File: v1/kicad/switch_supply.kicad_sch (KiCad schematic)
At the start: 12 parts, among them U11 ADG419BN, U12 ADG419BN, U7 ADG419BN

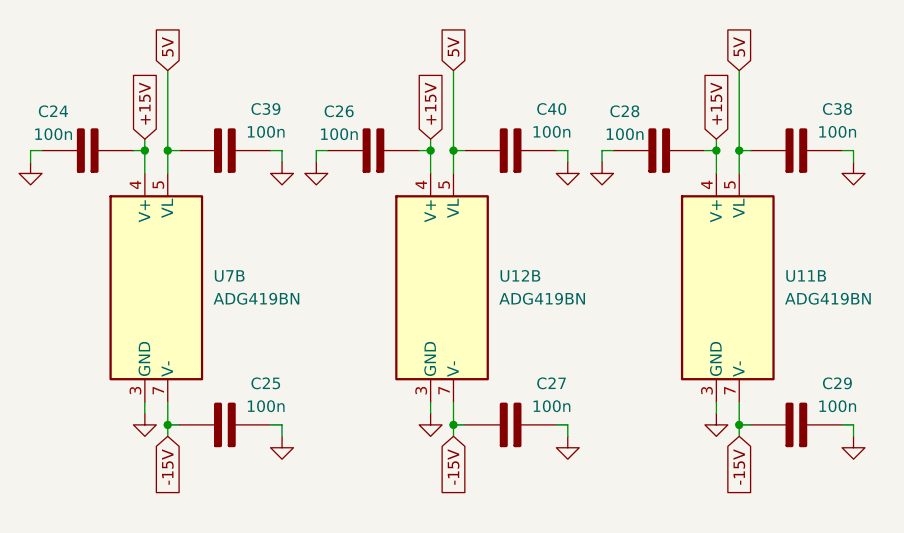
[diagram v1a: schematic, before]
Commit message: Adding KiKit multiboarding
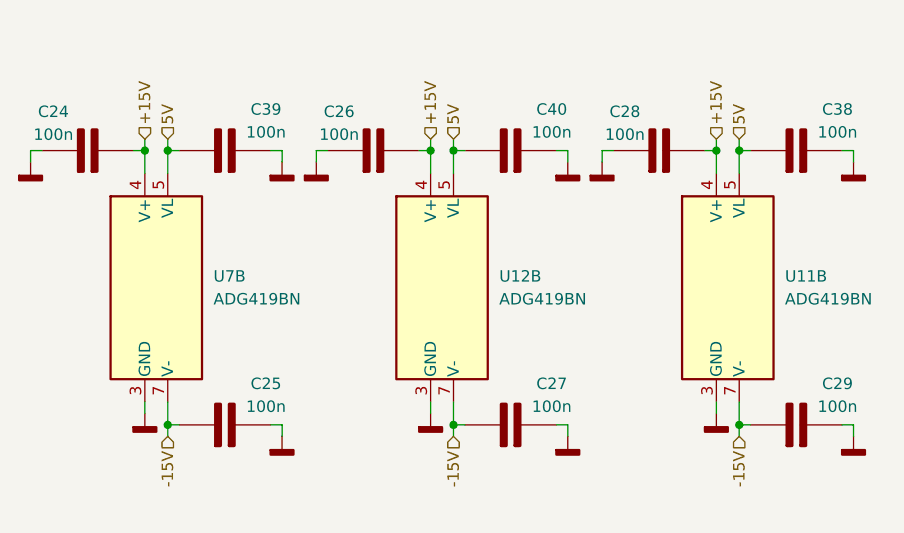
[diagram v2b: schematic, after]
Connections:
- net GND renamed GNDD

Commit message: Fixed mistakes and made making a BOM easier
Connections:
- net +15V: now also C24.2, C26.2, C28.2; no longer C24., C26., C28.
- net -15V: now also C25.1, C27.1, C29.1; no longer C25., C27., C29.
- net 5V: now also C38.1, C39.1, C40.1; no longer C38., C39., C40.
- net GNDD: now also C24.1, C25.2, C26.1, C27.2, C28.1, C29.2, C38.2, C39.2, C40.2; no longer C24., C25., C26., C27., C28., C29., C38., C39., C40.
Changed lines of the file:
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@@
 	)
 	(symbol
-		(lib_name "C_Basic_1")
 		(lib_id "custom:C_Basic")
 		(at 152.4 54.61 90)
@@
 			)
 		)
-		(pin ""
-		)
-		(pin ""
+		(pin "2"
+		)
+		(pin "1"
 		)
 		(instances
@@
 	)
 	(symbol
-		(lib_name "C_Basic_16")
 		(lib_id "custom:C_Basic")
 		(at 105.41 54.61 90)
@@
 			)
 		)
-		(pin ""
-		)
-		(pin ""
+		(pin "2"
+		)
+		(pin "1"
 		)
 		(instances
@@
 	)
 	(symbol
-		(lib_name "C_Basic_18")
 		(lib_id "custom:C_Basic")
 		(at 137.16 54.61 90)
@@
 			)
 		)
-		(pin ""
-		)
-		(pin ""
+		(pin "2"
+		)
+		(pin "1"
 		)
 		(instances
@@
 	)
 	(symbol
-		(lib_name "C_Basic_3")
 		(lib_id "custom:C_Basic")
 		(at 120.65 54.61 90)
@@
 			)
 		)
-		(pin ""
-		)
-		(pin ""
+		(pin "1"
+		)
+		(pin "2"
 		)
 		(instances
@@
 	)
 	(symbol
-		(lib_name "C_Basic_14")
 		(lib_id "custom:C_Basic")
 		(at 88.9 85.09 90)
@@
 			)
 		)
-		(pin ""
-		)
-		(pin ""
+		(pin "2"
+		)
+		(pin "1"
 		)
 		(instances
@@
 	)
 	(symbol
-		(lib_name "C_Basic_11")
 		(lib_id "custom:C_Basic")
 		(at 73.66 54.61 90)
@@
 			)
 		)
-		(pin ""
-		)
-		(pin ""
+		(pin "2"
+		)
+		(pin "1"
 		)
 		(instances
@@
 	)
 	(symbol
-		(lib_name "C_Basic_2")
 		(lib_id "custom:C_Basic")
 		(at 88.9 54.61 90)
@@
 			)
 		)
-		(pin ""
-		)
-		(pin ""
+		(pin "2"
+		)
+		(pin "1"
 		)
 		(instances
@@
 	)
 	(symbol
-		(lib_name "C_Basic_17")
 		(lib_id "custom:C_Basic")
 		(at 152.4 85.09 90)
@@
 			)
 		)
-		(pin ""
-		)
-		(pin ""
+		(pin "2"
+		)
+		(pin "1"
 		)
 		(instances
@@
 	)
 	(symbol
-		(lib_name "C_Basic_15")
 		(lib_id "custom:C_Basic")
 		(at 120.65 85.09 90)
@@
 			)
 		)
-		(pin ""
-		)
-		(pin ""
-		)
-		(instances
+		(pin "1"
+		)
+		(pin "2"
+		)
+		(instances
